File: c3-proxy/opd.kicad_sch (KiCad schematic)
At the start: 9 parts, among them U2 INA226

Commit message: style and logic fixes
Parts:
- added BZ1: SMT-0440-S-R, oresat-misc:SMT-0440-S-R, symbol Device:Buzzer
- added C7: 100nF, oresat-passives:0805-A, symbol Device:C_Small
- added D13: 1N4151WS, Diode_SMD:D_SOD-323, symbol oresat-diodes:1N4151WS-HE3
- added Q7: DMP2035UQ-7, Package_TO_SOT_SMD:SOT-23-3, symbol Simulation_SPICE:PMOS
- added R95: 10k, oresat-passives:0603-C-NOSILK, symbol Device:R_Small_US
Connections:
- net 3.3V: now also BZ1.1 (+), C7.1, D13.1, R95.1
- net GND: now also C7.2, Q7.1 (D)
- net at U2.3 (~{Alert}): now also Q7.2 (G), R95.2
- new net: BZ1.2 (-), D13.2, Q7.3 (S)
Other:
- note added: "CAUTION: WILL NOT WORK IN SPACE. Wait, no. Will work, can't hear. If you can't hear it, check if you're in space. Also, debug before you're in space. dummy...."
- note added: "F_res = 1.6kHz & 4-5.5 KHz"
- note added: "THEO'S OPTIONAL SPACE BUZZER!!11!"
- note added: "just in case"
- note added: "someone double check my transistor please"

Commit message: final layout and schematic touch ups
killed buzzer
deleted old folder
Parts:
- removed BZ1: SMT-0440-S-R, oresat-misc:SMT-0440-S-R, symbol Device:Buzzer
- removed D13: 1N4151WS, Diode_SMD:D_SOD-323, symbol oresat-diodes:1N4151WS-HE3
- removed Q7: DMP2035UQ-7, Package_TO_SOT_SMD:SOT-23-3, symbol Simulation_SPICE:PMOS
- removed R95: 10k, oresat-passives:0603-C-NOSILK, symbol Device:R_Small_US
- C7: DIST (none) -> DigiKey; DPN (none) -> 399-6856-1-ND; MFR (none) -> KEMET; MPN (none) -> C0603C104K5RACAUTO
- R16, R17, R18, R19, R20, R21, R22, R23: DIST (none) -> DigiKey; DPN (none) -> RMCF0603ZT0R00CT-ND; MFR (none) -> Stackpole Electronics; MPN (none) -> RMCF0603ZT0R00
- U2: DIST (none) -> DIgiKey; DPN (none) -> 296-29100-2-ND; MFR (none) -> Texas Instruments; MPN (none) -> INA226AIDGST
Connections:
- no-connect marks 0 -> 1
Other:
- note removed: "CAUTION: WILL NOT WORK IN SPACE. Wait, no. Will work, can't hear. If you can't hear it, check if you're in space. Also, debug before you're in space. dummy...."
- note removed: "F_res = 1.6kHz & 4-5.5 KHz"
- note removed: "THEO'S OPTIONAL SPACE BUZZER!!11!"
- note removed: "just in case"
- note removed: "someone double check my transistor please"

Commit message: did like... everything...
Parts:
- R16, R17, R18, R20, R21, R22, R23: value 0 -> 100
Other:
- note added: "choose I2C address with resistor network does not overlap with OPD address space INA226 goes from 0x40 - 0x4F OPD ranges from 0x08 - 0x3F"
- note removed: "choose I2C address with resistor network overlaps with possible OPD address space when A1=(SDA or SCL)"
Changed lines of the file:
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@@
 		)
 	)
-	(text "choose I2C address with resistor network\noverlaps with possible OPD address space when A1=(SDA or SCL)"
+	(text "choose I2C address with resistor network\ndoes not overlap with OPD address space\nINA226 goes from 0x40 - 0x4F\nOPD ranges from 0x08 - 0x3F "
 		(exclude_from_sim no)
-		(at 230.124 75.184 0)
+		(at 292.862 100.584 0)
 		(effects
 			(font
@@
 			)
 		)
-		(property "Value" "0"
+		(property "Value" "100"
 			(at 243.332 103.124 90)
 			(show_name no)
@@
 			)
 		)
-		(property "Value" "0"
+		(property "Value" "100"
 			(at 225.298 125.984 90)
 			(show_name no)
@@
 			)
 		)
-		(property "Value" "0"
+		(property "Value" "100"
 			(at 225.298 91.694 90)
 			(show_name no)
@@
 			)
 		)
-		(property "Value" "0"
+		(property "Value" "100"
 			(at 243.332 91.694 90)
 			(show_name no)
@@
 			)
 		)
-		(property "Value" "0"
+		(property "Value" "100"
 			(at 243.332 114.554 90)
 			(show_name no)
@@
 			)
 		)
-		(property "Value" "0"
+		(property "Value" "100"
 			(at 225.298 103.124 90)
 			(show_name no)
@@
 			)
 		)
-		(property "Value" "0"
+		(property "Value" "100"
 			(at 225.298 114.554 90)
 			(show_name no)

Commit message: v1.0 of the C3 Proxy sent off to fabrication.
Added makefile and README. Fixed a bunch of BOM issues, mostly just EOL and out of stock components. Fixed wrong footprints in the BOM, and switched diode from TH to SMT. Cleaned up some traces for funsies,
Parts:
- C7: value 100nF -> 100n; footprint oresat-passives:0805-A -> oresat-passives:0603-A
- R16, R17, R18, R20, R21, R22, R23: DPN RMCF0603ZT0R00CT-ND -> RMCF0603FT100RCT-ND; MPN RMCF0603ZT0R00 -> RMCF0603FT100R
- R19: value 0 -> 100; DPN RMCF0603ZT0R00CT-ND -> RMCF0603FT100RCT-ND; MPN RMCF0603ZT0R00 -> RMCF0603FT100R
- U2: DPN 296-29100-2-ND -> 296-29100-1-ND
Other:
- note added: "Default is 0x40 (0b100_0000)"
- note added: "INA226 Address Selection"
- note removed: "defaults to 0b100_0000"
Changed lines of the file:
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@@
 	(text "SCL"
 		(exclude_from_sim no)
-		(at 252.476 87.122 0)
+		(at 249.936 87.122 0)
 		(effects
 			(font
@@
 	(text "GND\n"
 		(exclude_from_sim no)
-		(at 252.984 121.412 0)
+		(at 250.444 121.412 0)
 		(effects
 			(font
@@
 	(text "SDA\n"
 		(exclude_from_sim no)
-		(at 252.476 98.298 0)
+		(at 249.936 98.298 0)
 		(effects
 			(font
 				(size 1.27 1.27)
+			)
+		)
+	)
+	(text "INA226 Address Selection"
+		(exclude_from_sim no)
+		(at 232.41 60.96 0)
+		(effects
+			(font
+				(size 1.27 1.27)
+				(thickness 0.254)
+				(bold yes)
 			)
 		)
@@
 	(text "see INA226 datasheet table 6-2 for possible combinations\n"
 		(exclude_from_sim no)
-		(at 291.592 107.95 0)
+		(at 233.426 72.644 0)
 		(effects
 			(font
@@
 		)
 	)
-	(text "defaults to 0b100_0000"
-		(exclude_from_sim no)
-		(at 290.83 112.268 0)
+	(text "Default is 0x40 (0b100_0000)"
+		(exclude_from_sim no)
+		(at 231.648 75.184 0)
 		(effects
 			(font
@@
 	(text "VS"
 		(exclude_from_sim no)
-		(at 252.476 109.728 0)
+		(at 249.936 109.728 0)
 		(effects
 			(font
@@
 	(text "choose I2C address with resistor network\ndoes not overlap with OPD address space\nINA226 goes from 0x40 - 0x4F\nOPD ranges from 0x08 - 0x3F "
 		(exclude_from_sim no)
-		(at 292.862 100.584 0)
+		(at 232.41 67.31 0)
 		(effects
 			(font
@@
 			)
 		)
-		(property "Description" "0 Ohms Jumper Chip Resistor 0603 (1608 Metric) Automotive AEC-Q200 Thick Film"
+		(property "Description" "100 Ohms ±1% 0.1W, 1/10W Chip Resistor 0603 (1608 Metric) Automotive AEC-Q200 Thick Film"
 			(at 241.3 97.79 0)
 			(hide yes)
@@
 			)
 		)
-		(property "DPN" "RMCF0603ZT0R00CT-ND"
+		(property "DPN" "RMCF0603FT100RCT-ND"
 			(at 241.3 97.79 90)
 			(hide yes)
@@
 			)
 		)
-		(property "MPN" "RMCF0603ZT0R00"
+		(property "MPN" "RMCF0603FT100R"
 			(at 241.3 97.79 90)
 			(hide yes)
@@
 			)
 		)
-		(property "Description" "0 Ohms Jumper Chip Resistor 0603 (1608 Metric) Automotive AEC-Q200 Thick Film"
+		(property "Description" "100 Ohms ±1% 0.1W, 1/10W Chip Resistor 0603 (1608 Metric) Automotive AEC-Q200 Thick Film"
 			(at 227.33 120.65 0)
 			(hide yes)
@@
 			)
 		)
-		(property "DPN" "RMCF0603ZT0R00CT-ND"
+		(property "DPN" "RMCF0603FT100RCT-ND"
 			(at 227.33 120.65 90)
 			(hide yes)
@@
 			)
 		)
-		(property "MPN" "RMCF0603ZT0R00"
+		(property "MPN" "RMCF0603FT100R"
 			(at 227.33 120.65 90)
 			(hide yes)
@@
 			)
 		)
-		(property "Value" "0"
+		(property "Value" "100"
 			(at 243.332 125.984 90)
 			(show_name no)
@@
 			)
 		)
-		(property "Description" "0 Ohms Jumper Chip Resistor 0603 (1608 Metric) Automotive AEC-Q200 Thick Film"
+		(property "Description" "100 Ohms ±1% 0.1W, 1/10W Chip Resistor 0603 (1608 Metric) Automotive AEC-Q200 Thick Film"
 			(at 241.3 120.65 0)
 			(hide yes)
@@
 			)
 		)
-		(property "DPN" "RMCF0603ZT0R00CT-ND"
+		(property "DPN" "RMCF0603FT100RCT-ND"
 			(at 241.3 120.65 90)
 			(hide yes)
@@
 			)
 		)
-		(property "MPN" "RMCF0603ZT0R00"
+		(property "MPN" "RMCF0603FT100R"
 			(at 241.3 120.65 90)
 			(hide yes)
@@
 			)
 		)
-		(property "DPN" "296-29100-2-ND"
+		(property "DPN" "296-29100-1-ND"
 			(at 177.8 147.32 0)
 			(hide yes)
@@
 			)
 		)
-		(property "Description" "0 Ohms Jumper Chip Resistor 0603 (1608 Metric) Automotive AEC-Q200 Thick Film"
+		(property "Description" "100 Ohms ±1% 0.1W, 1/10W Chip Resistor 0603 (1608 Metric) Automotive AEC-Q200 Thick Film"
 			(at 227.33 86.36 0)
 			(hide yes)
@@
 			)
 		)
-		(property "DPN" "RMCF0603ZT0R00CT-ND"
+		(property "DPN" "RMCF0603FT100RCT-ND"
 			(at 227.33 86.36 90)
 			(hide yes)
@@
 			)
 		)
-		(property "MPN" "RMCF0603ZT0R00"
+		(property "MPN" "RMCF0603FT100R"
 			(at 227.33 86.36 90)
 			(hide yes)
@@
 			)
 		)
-		(property "Value" "100nF"
+		(property "Value" "100n"
 			(at 160.274 127 0)
 			(show_name no)
@@
 			)
 		)
-		(property "Footprint" "oresat-passives:0805-A"
+		(property "Footprint" "oresat-passives:0603-A"
 			(at 168.91 125.73 0)
 			(hide yes)
@@
 			)
 		)
-		(property "Description" "0 Ohms Jumper Chip Resistor 0603 (1608 Metric) Automotive AEC-Q200 Thick Film"
+		(property "Description" "100 Ohms ±1% 0.1W, 1/10W Chip Resistor 0603 (1608 Metric) Automotive AEC-Q200 Thick Film"
 			(at 241.3 86.36 0)
 			(hide yes)
@@
 			)
 		)
-		(property "DPN" "RMCF0603ZT0R00CT-ND"
+		(property "DPN" "RMCF0603FT100RCT-ND"
 			(at 241.3 86.36 90)
 			(hide yes)
@@
 			)
 		)
-		(property "MPN" "RMCF0603ZT0R00"
+		(property "MPN" "RMCF0603FT100R"
 			(at 241.3 86.36 90)
 			(hide yes)
@@
 			)
 		)
-		(property "Description" "0 Ohms Jumper Chip Resistor 0603 (1608 Metric) Automotive AEC-Q200 Thick Film"
+		(property "Description" "100 Ohms ±1% 0.1W, 1/10W Chip Resistor 0603 (1608 Metric) Automotive AEC-Q200 Thick Film"
 			(at 241.3 109.22 0)
 			(hide yes)
@@
 			)
 		)
-		(property "DPN" "RMCF0603ZT0R00CT-ND"
+		(property "DPN" "RMCF0603FT100RCT-ND"
 			(at 241.3 109.22 90)
 			(hide yes)
@@
 			)
 		)
-		(property "MPN" "RMCF0603ZT0R00"
+		(property "MPN" "RMCF0603FT100R"
 			(at 241.3 109.22 90)
 			(hide yes)
@@
 			)
 		)
-		(property "Description" "0 Ohms Jumper Chip Resistor 0603 (1608 Metric) Automotive AEC-Q200 Thick Film"
+		(property "Description" "100 Ohms ±1% 0.1W, 1/10W Chip Resistor 0603 (1608 Metric) Automotive AEC-Q200 Thick Film"
 			(at 227.33 97.79 0)
 			(hide yes)
@@
 			)
 		)
-		(property "DPN" "RMCF0603ZT0R00CT-ND"
+		(property "DPN" "RMCF0603FT100RCT-ND"
 			(at 227.33 97.79 90)
 			(hide yes)
@@
 			)
 		)
-		(property "MPN" "RMCF0603ZT0R00"
+		(property "MPN" "RMCF0603FT100R"
 			(at 227.33 97.79 90)
 			(hide yes)
@@
 			)
 		)
-		(property "Description" "0 Ohms Jumper Chip Resistor 0603 (1608 Metric) Automotive AEC-Q200 Thick Film"
+		(property "Description" "100 Ohms ±1% 0.1W, 1/10W Chip Resistor 0603 (1608 Metric) Automotive AEC-Q200 Thick Film"
 			(at 227.33 109.22 0)
 			(hide yes)
@@
 			)
 		)
-		(property "DPN" "RMCF0603ZT0R00CT-ND"
+		(property "DPN" "RMCF0603FT100RCT-ND"
 			(at 227.33 109.22 90)
 			(hide yes)
@@
 			)
 		)
-		(property "MPN" "RMCF0603ZT0R00"
+		(property "MPN" "RMCF0603FT100R"
 			(at 227.33 109.22 90)
 			(hide yes)

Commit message: decreased size to fit in EU, transistor orientation
changed DC jack to be edge connected.
adjusted layout in top-right corner to still fit mounting hole.
fixed transistor orientation by switching to GSD symbols
moved SW2 and clarified silkscreen with boxes
changed via sizes to be standardized
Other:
- title: Flatsat Interface Card -> c3-Proxy card
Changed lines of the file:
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@@
 	(paper "B")
 	(title_block
-		(title "Flatsat Interface Card")
-		(date "2026-06-29")
+		(title "c3-Proxy card")
+		(date "2026-09-07")
 		(rev "${REVISION}")
 		(company "Portland State Aerospace Society")

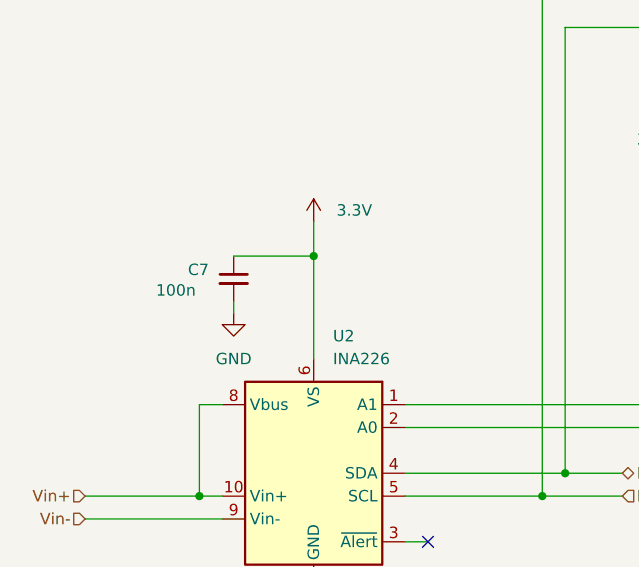
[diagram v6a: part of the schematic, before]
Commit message: changed footprints in schematic
so that "update from schematic" doesn't kill my baby resistors
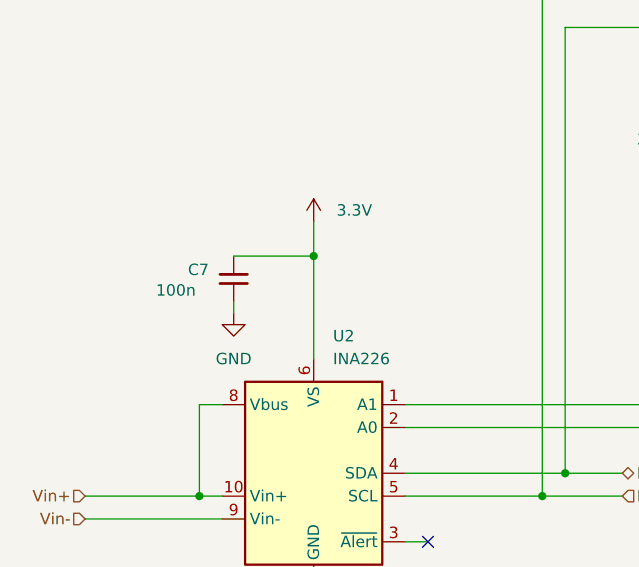
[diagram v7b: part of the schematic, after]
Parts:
- C7: footprint oresat-passives:0603-A -> oresat-passives:0603-C-NOSILK; DIST DigiKey -> (none); DPN 399-6856-1-ND -> (none); MFR KEMET -> (none); MPN C0603C104K5RACAUTO -> (none)
- R16, R17, R18, R19, R20, R21, R22, R23: footprint oresat-passives:0603-A -> oresat-passives:0603-C-NOSILK
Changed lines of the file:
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@@
 			)
 		)
-		(property "Footprint" "oresat-passives:0603-A"
+		(property "Footprint" "oresat-passives:0603-C-NOSILK"
 			(at 241.3 97.79 0)
 			(hide yes)
@@
 			)
 		)
-		(property "Footprint" "oresat-passives:0603-A"
+		(property "Footprint" "oresat-passives:0603-C-NOSILK"
 			(at 227.33 120.65 0)
 			(hide yes)
@@
 			)
 		)
-		(property "Footprint" "oresat-passives:0603-A"
+		(property "Footprint" "oresat-passives:0603-C-NOSILK"
 			(at 241.3 120.65 0)
 			(hide yes)
@@
 			)
 		)
-		(property "Footprint" "oresat-passives:0603-A"
+		(property "Footprint" "oresat-passives:0603-C-NOSILK"
 			(at 227.33 86.36 0)
 			(hide yes)
@@
 			)
 		)
-		(property "Footprint" "oresat-passives:0603-A"
+		(property "Footprint" "oresat-passives:0603-C-NOSILK"
 			(at 168.91 125.73 0)
 			(hide yes)
@@
 			)
 		)
-		(property "Datasheet" "https://search.kemet.com/download/specsheet/C0603C104K5RACAUTO"
+		(property "Datasheet" ""
 			(at 168.91 125.73 0)
 			(hide yes)
@@
 			)
 		)
-		(property "Description" "0.1 µF ±10% 50V Ceramic Capacitor X7R 0603 (1608 Metric)"
-			(at 168.91 125.73 0)
-			(hide yes)
-			(show_name no)
-			(do_not_autoplace no)
-			(effects
-				(font
-					(size 1.27 1.27)
-				)
-			)
-		)
-		(property "DIST" "DigiKey"
-			(at 168.91 125.73 0)
-			(hide yes)
-			(show_name no)
-			(do_not_autoplace no)
-			(effects
-				(font
-					(size 1.27 1.27)
-				)
-			)
-		)
-		(property "DPN" "399-6856-1-ND"
-			(at 168.91 125.73 0)
-			(hide yes)
-			(show_name no)
-			(do_not_autoplace no)
-			(effects
-				(font
-					(size 1.27 1.27)
-				)
-			)
-		)
-		(property "MFR" "KEMET"
-			(at 168.91 125.73 0)
-			(hide yes)
-			(show_name no)
-			(do_not_autoplace no)
-			(effects
-				(font
-					(size 1.27 1.27)
-				)
-			)
-		)
-		(property "MPN" "C0603C104K5RACAUTO"
-			(at 168.91 125.73 0)
+		(property "Description" "Unpolarized capacitor, small symbol"
+			(at 168.91 135.89 0)
 			(hide yes)
 			(show_name no)
@@
 			)
 		)
-		(property "Footprint" "oresat-passives:0603-A"
+		(property "Footprint" "oresat-passives:0603-C-NOSILK"
 			(at 241.3 86.36 0)
 			(hide yes)
@@
 			)
 		)
-		(property "Footprint" "oresat-passives:0603-A"
+		(property "Footprint" "oresat-passives:0603-C-NOSILK"
 			(at 241.3 109.22 0)
 			(hide yes)
@@
 			)
 		)
-		(property "Footprint" "oresat-passives:0603-A"
+		(property "Footprint" "oresat-passives:0603-C-NOSILK"
 			(at 227.33 97.79 0)
 			(hide yes)
@@
 			)
 		)
-		(property "Footprint" "oresat-passives:0603-A"
+		(property "Footprint" "oresat-passives:0603-C-NOSILK"
 			(at 227.33 109.22 0)
 			(hide yes)

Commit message: fixed BOM, silk art scale
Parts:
- C7: DIST (none) -> DigiKey; DPN (none) -> 399-6856-1-ND; MFR (none) -> KEMET; MPN (none) -> C0603C104K5RACAUTO
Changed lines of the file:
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@@
 			)
 		)
-		(property "Datasheet" ""
+		(property "Datasheet" "https://search.kemet.com/download/specsheet/C0603C104K5RACAUTO"
 			(at 168.91 125.73 0)
 			(hide yes)
@@
 			)
 		)
-		(property "Description" "Unpolarized capacitor, small symbol"
+		(property "Description" "0.1 µF ±10% 50V Ceramic Capacitor X7R 0603 (1608 Metric)"
 			(at 168.91 135.89 0)
 			(hide yes)
 			(show_name no)
+			(do_not_autoplace no)
+			(effects
+				(font
+					(size 1.27 1.27)
+				)
+			)
+		)
+		(property "DIST" "DigiKey"
+			(at 168.91 125.73 0)
+			(hide yes)
+			(show_name no)
+			(do_not_autoplace no)
+			(effects
+				(font
+					(size 1.27 1.27)
+				)
+			)
+		)
+		(property "DPN" "399-6856-1-ND"
+			(at 168.91 125.73 0)
+			(hide yes)
+			(show_name no)
+			(do_not_autoplace no)
+			(effects
+				(font
+					(size 1.27 1.27)
+				)
+			)
+		)
+		(property "MFR" "KEMET"
+			(at 168.91 125.73 0)
+			(hide yes)
+			(show_name no)
+			(do_not_autoplace no)
+			(effects
+				(font
+					(size 1.27 1.27)
+				)
+			)
+		)
+		(property "MPN" "C0603C104K5RACAUTO"
+			(at 168.91 125.73 0)
+			(hide yes)
+			(show_name no)
